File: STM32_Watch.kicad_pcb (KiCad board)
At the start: 2 copper layers, 35 parts, among them Q1 AO3401A, U1 STM32L031K6Ux, U2 LIS2MDL

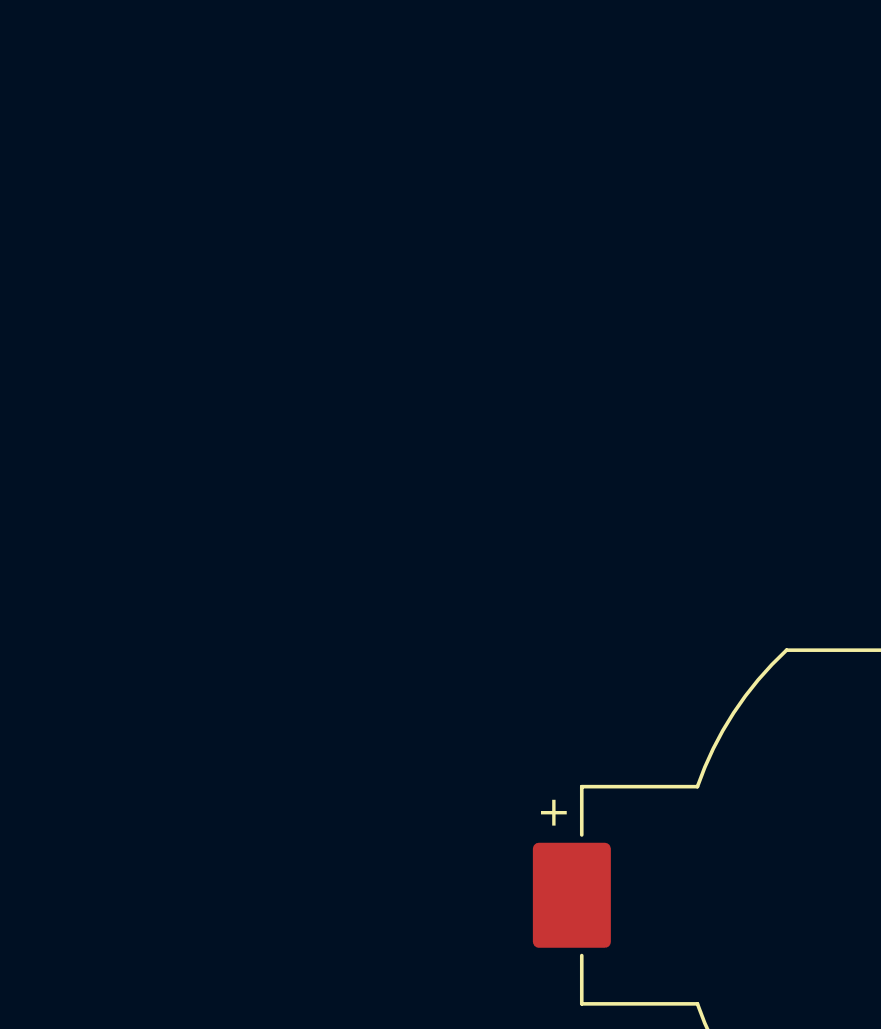
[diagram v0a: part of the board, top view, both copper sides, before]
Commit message: Added net lables & ERC fixes
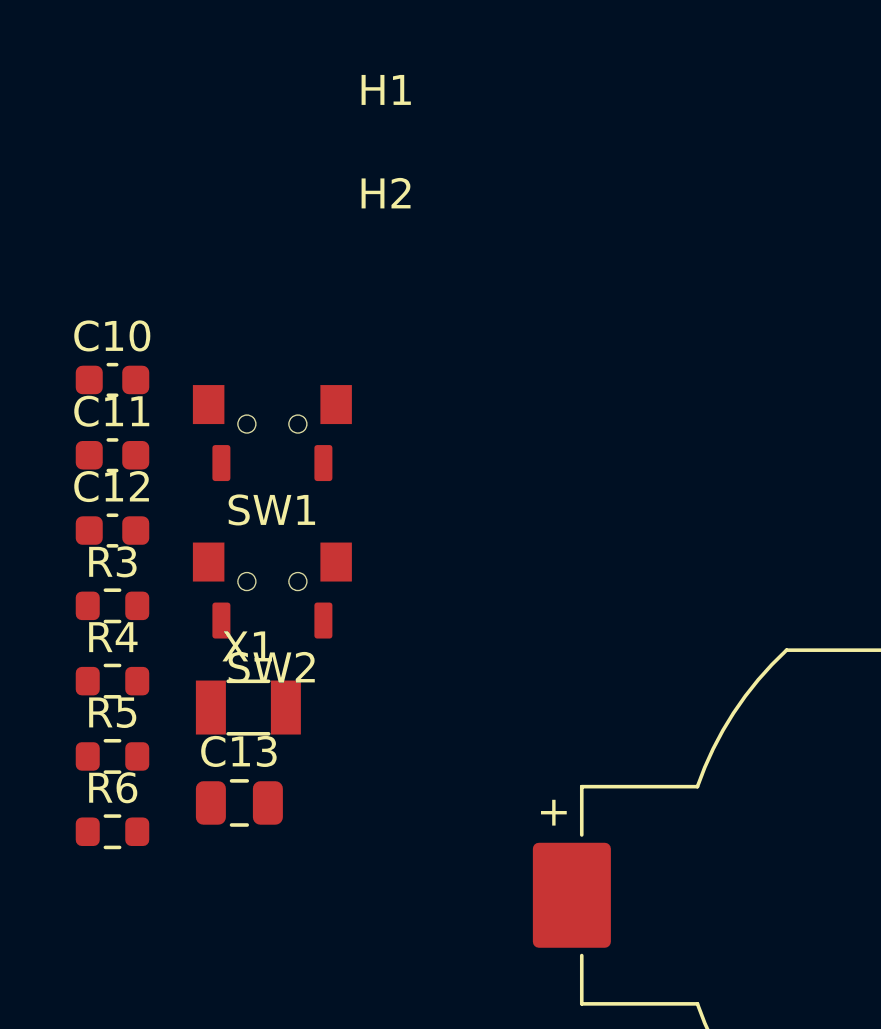
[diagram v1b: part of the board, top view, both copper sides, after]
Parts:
- added C10: 100n, Capacitor_SMD:C_0603_1608Metric, F.Cu at (119.8, 76.7)
- added C11: 100n, Capacitor_SMD:C_0603_1608Metric, F.Cu at (119.8, 79.2)
- added C12: 100n, Capacitor_SMD:C_0603_1608Metric, F.Cu at (119.8, 81.7)
- added C13: 10u, Capacitor_SMD:C_0805_2012Metric, F.Cu at (124.0, 90.8)
- added H1: MountingHole, STM32_Watch:StrapsConnection_20mm, F.Cu at (128.9, 70.2)
- added H2: MountingHole, STM32_Watch:StrapsConnection_20mm, F.Cu at (128.9, 73.7)
- added R3: 1M, Resistor_SMD:R_0603_1608Metric, F.Cu at (119.8, 84.2)
- added R4: 10k, Resistor_SMD:R_0603_1608Metric, F.Cu at (119.8, 86.7)
- added R5: 10k, Resistor_SMD:R_0603_1608Metric, F.Cu at (119.8, 89.2)
- added R6: 10k, Resistor_SMD:R_0603_1608Metric, F.Cu at (119.8, 91.7)
- added SW1: SW_Push, STM32_Watch:SHOU_HAN_TS24CA, F.Cu at (125.2, 78.1)
- added SW2: SW_Push, STM32_Watch:SHOU_HAN_TS24CA, F.Cu at (125.2, 83.4)
- added X1: 32.768k, STM32_Watch:Crystal_SMD_3215-2pin_3.2x1.5mm, F.Cu at (124.3, 87.6)
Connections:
- D1 pad 2: unconnected-(D1-A-Pad2) -> LED_1
- D10 pad 2: unconnected-(D10-A-Pad2) -> LED_10
- D11 pad 2: unconnected-(D11-A-Pad2) -> LED_11
- D12 pad 2: unconnected-(D12-A-Pad2) -> LED_12
- D2 pad 2: unconnected-(D2-A-Pad2) -> LED_2
- D3 pad 2: unconnected-(D3-A-Pad2) -> LED_3
- D4 pad 2: unconnected-(D4-A-Pad2) -> LED_4
- D5 pad 2: unconnected-(D5-A-Pad2) -> LED_5
- D6 pad 2: unconnected-(D6-A-Pad2) -> LED_6
- D7 pad 2: unconnected-(D7-A-Pad2) -> LED_7
- D8 pad 2: unconnected-(D8-A-Pad2) -> LED_8
- D9 pad 2: unconnected-(D9-A-Pad2) -> LED_9
- Q1 pad 1: unconnected-(Q1-G-Pad1) -> Net-(Q1-G)
- Q1 pad 2: unconnected-(Q1-S-Pad2) -> /VDD_MAG
- Q1 pad 3: unconnected-(Q1-D-Pad3) -> VDD
- U1 pad 10: unconnected-(U1-PA4-Pad10) -> LED_7
- U1 pad 11: unconnected-(U1-PA5-Pad11) -> LED_6
- U1 pad 12: unconnected-(U1-PA6-Pad12) -> LED_5
- U1 pad 13: unconnected-(U1-PA7-Pad13) -> I2C_INT
- U1 pad 14: unconnected-(U1-PB0-Pad14) -> SW1
- U1 pad 15: unconnected-(U1-PB1-Pad15) -> SW2
- U1 pad 16: unconnected-(U1-PB2-Pad16) -> MAG_EN
- U1 pad 18: unconnected-(U1-PA8-Pad18) -> LED_4
- U1 pad 21: unconnected-(U1-PA11-Pad21) -> LED_3
- U1 pad 22: unconnected-(U1-PA12-Pad22) -> LED_2
- U1 pad 28: unconnected-(U1-PB5-Pad28) -> LED_1
- U1 pad 29: unconnected-(U1-PB6-Pad29) -> LED_12
- U1 pad 30: unconnected-(U1-PB7-Pad30) -> LED_11
- U1 pad 32: unconnected-(U1-PB8-Pad32) -> LED_10
- U1 pad 6: unconnected-(U1-PA0-Pad6) -> LED_9
- U1 pad 7: unconnected-(U1-PA1-Pad7) -> LED_8
- U2 pad 1: unconnected-(U2-SCL/SPC-Pad1) -> I2C_SCL
- U2 pad 10: unconnected-(U2-Vdd_IO-Pad10) -> /VDD_MAG
- U2 pad 3: unconnected-(U2-~{CS}-Pad3) -> /VDD_MAG
- U2 pad 4: unconnected-(U2-SDA/SDI/SDO-Pad4) -> I2C_SDA
- U2 pad 5: unconnected-(U2-C1-Pad5) -> Net-(U2-C1)
- U2 pad 6: Net-(U2-GND-Pad6) -> GND
- U2 pad 7: unconnected-(U2-DRDY-Pad7) -> I2C_INT
- U2 pad 8: Net-(U2-GND-Pad6) -> GND
- U2 pad 9: unconnected-(U2-Vdd-Pad9) -> /VDD_MAG

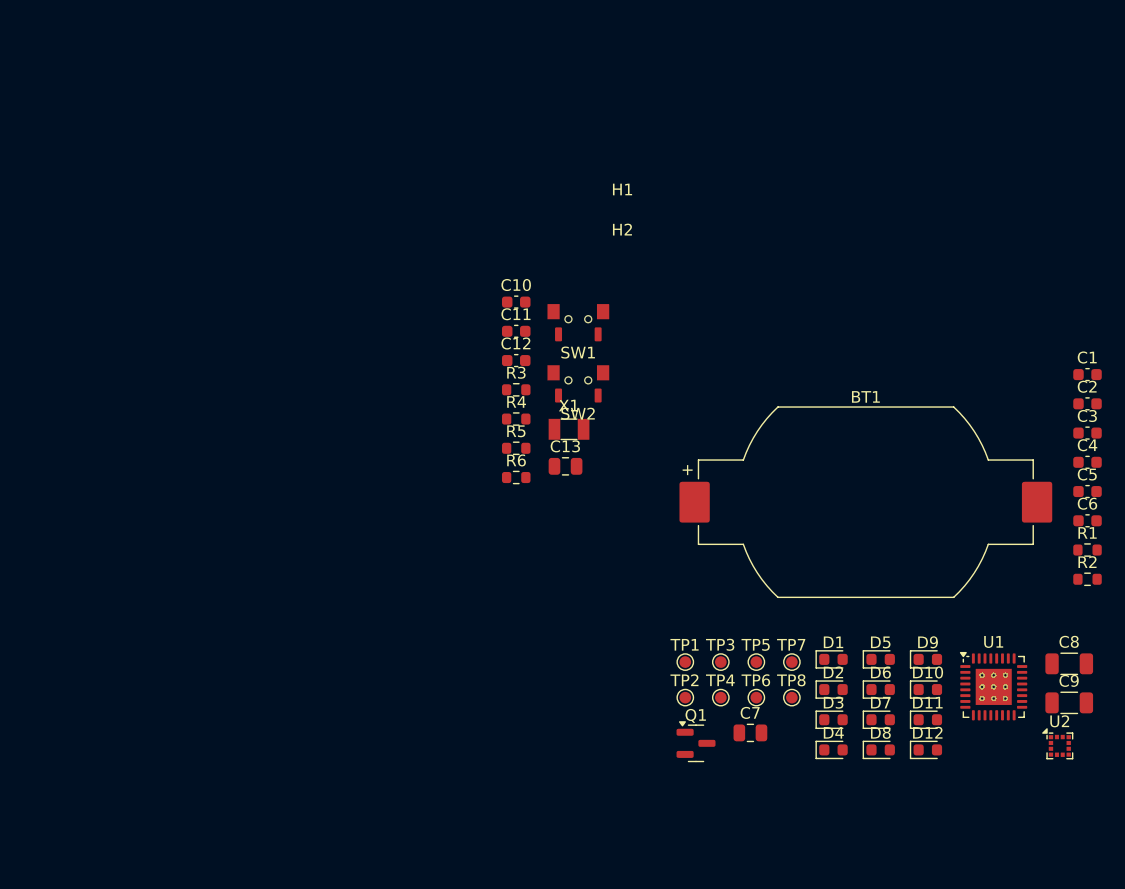
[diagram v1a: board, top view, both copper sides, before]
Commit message: Added ALSENS for ambient light measurments
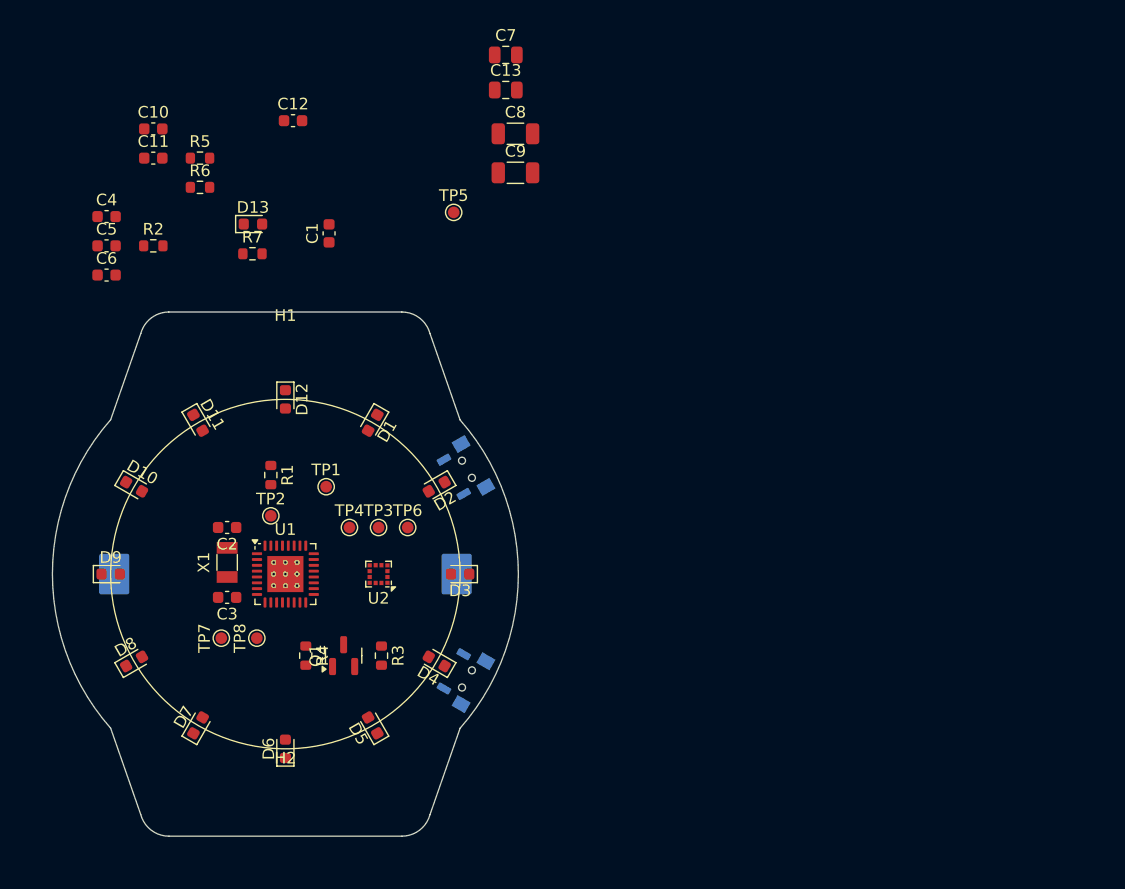
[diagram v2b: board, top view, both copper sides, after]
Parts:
- added D13: LED, LED_SMD:LED_0603_1608Metric, F.Cu at (97.2, 70.0)
- added R7: 1M, Resistor_SMD:R_0603_1608Metric, F.Cu at (97.2, 72.5)
- BT1, SW1, SW2: moved to B.Cu
- X1: footprint STM32_Watch:Crystal_SMD_3215-2pin_3.2x1.5mm -> Crystal:Crystal_SMD_3215-2Pin_3.2x1.5mm
- moved C4 86.8 mm to (84.7, 69.3)
- moved C5 86.8 mm to (84.7, 71.8)
- moved C6 86.8 mm to (84.7, 74.3)
- moved R2 85.2 mm to (88.7, 71.8)
- moved C3 75.2 mm to (95.0, 102.0), turned to 180 degrees
- moved C2 74.6 mm to (95.0, 96.0), turned to 180 degrees
- moved D9 70.5 mm to (85.0, 100.0)
- moved R1 70.4 mm to (98.8, 91.5), turned to -90 degrees
- moved D10 70.3 mm to (87.0, 92.5), turned to -30 degrees
- moved D11 67.6 mm to (92.5, 87.0), turned to -60 degrees
- moved C1 66.2 mm to (103.8, 70.8), turned to 90 degrees
- moved C8 65.8 mm to (119.8, 62.2)
- moved C9 65.8 mm to (119.8, 65.5)
- moved D8 64.5 mm to (87.0, 107.5), turned to 30 degrees
- moved D12 62.8 mm to (100.0, 85.0), turned to -90 degrees
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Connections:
- U1 pad 13: I2C_INT -> unconnected-(U1-PA7-Pad13)
- U1 pad 21: LED_3 -> I2C_INT
- U1 pad 22: LED_2 -> LED_3
- U1 pad 25: unconnected-(U1-PA15-Pad25) -> LED_2
- U1 pad 27: unconnected-(U1-PB4-Pad27) -> /ALSENS
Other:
- board outline added: 40 x 45 mm

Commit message: Realigned components & Removed boot TP
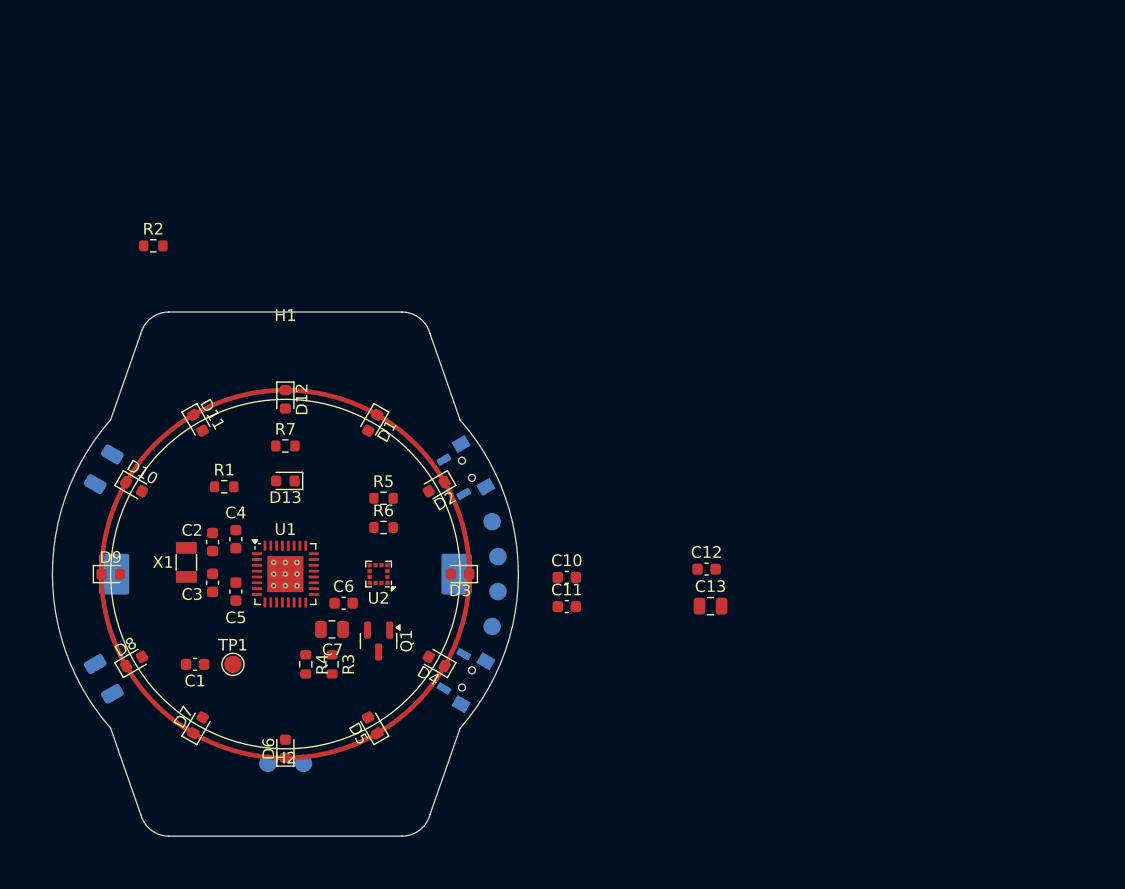
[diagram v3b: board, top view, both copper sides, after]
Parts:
- removed TP2: TestPoint_Small, TestPoint:TestPoint_Pad_D1.0mm
- C8, C9: moved to B.Cu
- TP1: footprint TestPoint:TestPoint_Pad_D1.0mm -> TestPoint:TestPoint_Pad_D1.5mm
- TP3, TP4, TP5, TP6, TP7, TP8: footprint TestPoint:TestPoint_Pad_D1.0mm -> TestPoint:TestPoint_Pad_D1.5mm; moved to B.Cu
- moved C9 56.0 mm to (84.4, 109.0), turned to 120 degrees
- moved C10 52.4 mm to (124.2, 100.3)
- moved C11 52.4 mm to (124.2, 102.8)
- moved C12 52.4 mm to (136.2, 99.6)
- moved C7 51.5 mm to (104.0, 104.8)
- moved C13 47.7 mm to (136.5, 102.8)
- moved C8 45.6 mm to (84.4, 91.0), turned to -120 degrees
- moved C1 38.7 mm to (92.2, 107.8), turned to 180 degrees
- moved TP5 35.7 mm to (117.8, 104.5), turned to 180 degrees
- moved C6 34.8 mm to (105.0, 102.5)
- moved R6 33.2 mm to (108.4, 96.0)
- moved R5 33.2 mm to (108.4, 93.5)
- moved C5 31.7 mm to (95.8, 101.5), turned to -90 degrees
- moved C4 29.8 mm to (95.8, 97.0), turned to 90 degrees
- moved D13 22.2 mm to (100.0, 92.0), turned to 180 degrees
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
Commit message: IMU instead of a compass
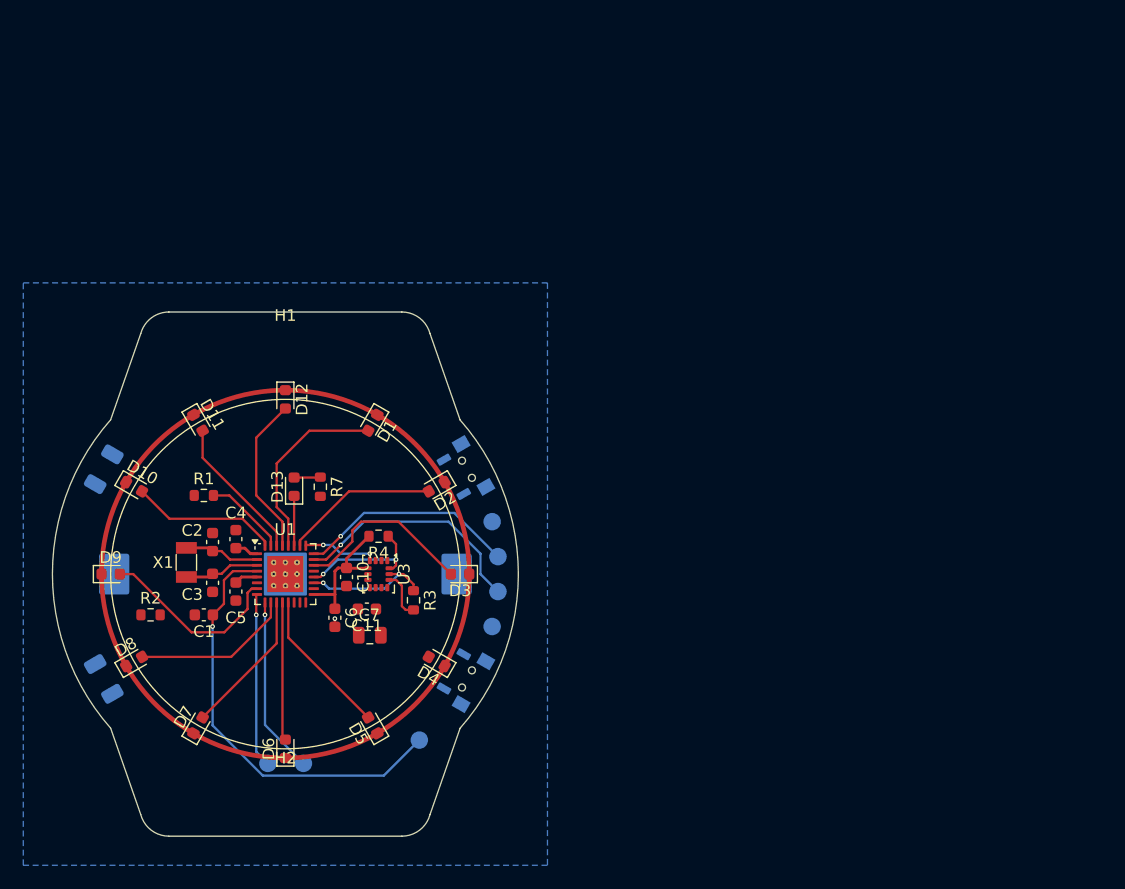
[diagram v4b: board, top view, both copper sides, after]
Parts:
- removed C12: 100n, Capacitor_SMD:C_0603_1608Metric
- removed C13: 10u, Capacitor_SMD:C_0805_2012Metric
- removed Q1: AO3401A, Package_TO_SOT_SMD:SOT-23
- removed R5, R6: 10k, Resistor_SMD:R_0603_1608Metric
- removed U2: LIS2MDL, Package_LGA:LGA-12_2x2mm_P0.5mm
- added U3: LSM6DS3, Package_LGA:LGA-14_3x2.5mm_P0.5mm_LayoutBorder3x4y, F.Cu at (108.0, 100.0)
- R3: value 1M -> 10k
- TP1: moved to B.Cu
- moved R2 31.7 mm to (88.4, 103.5)
- moved C10 18.9 mm to (105.2, 100.2), turned to -90 degrees
- moved TP1 17.3 mm to (111.5, 114.2), turned to 180 degrees
- moved C11 17.2 mm to (107.0, 103.0), turned to 180 degrees
- moved R4 12.7 mm to (108.0, 96.8), turned to 180 degrees
- moved R3 8.90 mm to (111.0, 102.2)
- moved R7 4.61 mm to (103.0, 92.5), turned to -90 degrees
- moved C1 4.32 mm to (93.0, 103.5)
- moved C7 3.29 mm to (107.2, 105.2), turned to 180 degrees
- moved R1 1.90 mm to (93.0, 93.2)
- moved C6 1.46 mm to (104.2, 103.8), turned to -90 degrees
- moved D13 0.90 mm to (100.8, 92.5), turned to 90 degrees
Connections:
- C10 pad 1: /VDD_MAG -> VDD
- C11 pad 1: Net-(U2-C1) -> VDD
- R3 pad 1: VDD -> I2C_SCL
- R3 pad 2: Net-(Q1-G) -> VDD
- R4 pad 1: MAG_EN -> I2C_SDA
- R4 pad 2: Net-(Q1-G) -> VDD
- U1 pad 10: LED_7 -> LED_8
- U1 pad 11: LED_6 -> LED_7
- U1 pad 12: LED_5 -> LED_6
- U1 pad 13: unconnected-(U1-PA7-Pad13) -> LED_5
- U1 pad 16: MAG_EN -> IMU_INT2
- U1 pad 21: I2C_INT -> unconnected-(U1-PA11-Pad21)
- U1 pad 25: LED_2 -> IMU_INT1
- U1 pad 26: unconnected-(U1-PB3-Pad26) -> LED_2
- U1 pad 6: LED_9 -> unconnected-(U1-PA0-Pad6)
- U1 pad 7: LED_8 -> LED_9
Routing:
- net /NRST: track 0.00 -> 36.8 mm, vias 0 -> 1
- net /SWDIO: track 0.00 -> 20.7 mm, vias 0 -> 1
- net VDD: track 0.00 -> 19.7 mm
- net /SWCLK: track 0.00 -> 18.8 mm, vias 0 -> 1
- net LED_1: track 0.00 -> 16.5 mm
- net LED_9: track 0.00 -> 16.2 mm
- net LED_3: track 0.00 -> 15.8 mm
- net /UART_RX: track 0.00 -> 15.2 mm, vias 0 -> 1
- net /UART_TX: track 0.00 -> 14.9 mm, vias 0 -> 1
- net LED_12: track 0.00 -> 13.7 mm
- net LED_8: track 0.00 -> 13.7 mm
- net LED_2: track 0.00 -> 13.3 mm
- net LED_10: track 0.00 -> 12.7 mm
- net LED_5: track 0.00 -> 12.7 mm
- net LED_7: track 0.00 -> 12.5 mm
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- added copper zone on B.Cu, net GND

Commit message: Rearanged mcu pins & Routed
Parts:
- moved TP7 1.31 mm to (98.5, 114.9)
- moved TP8 1.31 mm to (101.5, 114.9)
- moved R2 1.21 mm to (87.8, 104.5)
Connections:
- net Net-(D1-K) renamed /LED-
- U1 pad 14: SW1 -> SW2
- U1 pad 15: SW2 -> SW1
- U1 pad 16: IMU_INT2 -> LED_4
- U1 pad 18: LED_4 -> IMU_INT2
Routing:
- net VDD: track 19.7 -> 89.9 mm, vias 0 -> 5
- net GND: track 0.70 -> 29.3 mm, vias 1 -> 106
- net SW2: track 0.00 -> 17.8 mm, vias 0 -> 1
- net SW1: track 0.00 -> 14.5 mm, vias 0 -> 1
- net LED_4: track 0.00 -> 13.0 mm
- net IMU_INT2: track 0.00 -> 6.48 mm, vias 0 -> 2
- net LED_8: track 13.7 -> 18.5 mm
- net LED_9: track 16.2 -> 20.2 mm
- net LED_7: track 12.5 -> 14.6 mm
- net /UART_TX: track 14.9 -> 13.6 mm
- net /UART_RX: track 15.2 -> 13.9 mm
- net LED_12: track 13.7 -> 12.7 mm
- net LED_10: track 12.7 -> 13.3 mm
- net /BOOT: track 7.16 -> 7.70 mm
- added copper zone on F.Cu, net GND
